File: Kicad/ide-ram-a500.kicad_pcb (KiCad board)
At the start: 2 copper layers, 82.5 x 34.9 mm, 27 parts, among them J1 power, J2 LED, J3 LED2, J4 INT2OVR, J5 INT2, J6 JTAG, J7 IDE, U1 68000D socket, U2 XC95144XL-TQ100, U3 SPX3819M5-L-3-3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

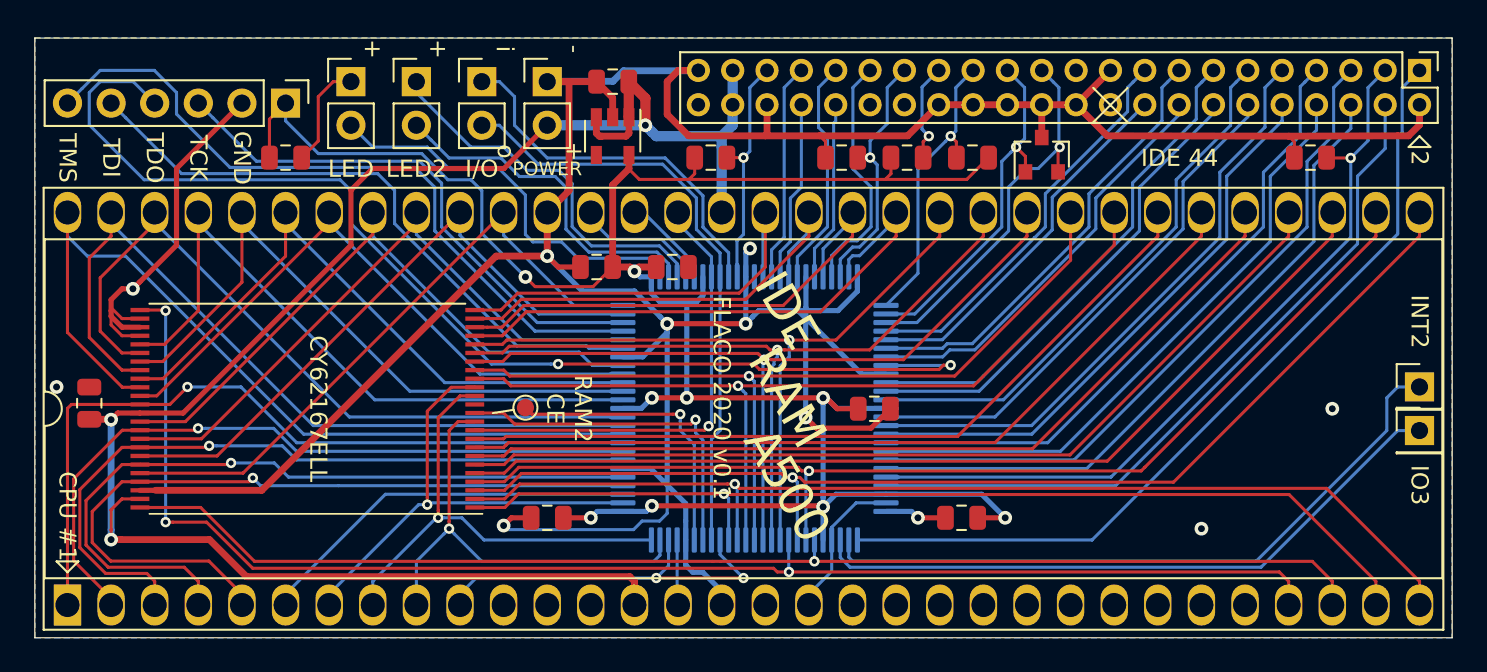
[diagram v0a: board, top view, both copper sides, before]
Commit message: Updated CPLD code with new autoconfig, new ranger-maprom, rewritten IDE ; new MapROM software ; 0.2 hardware
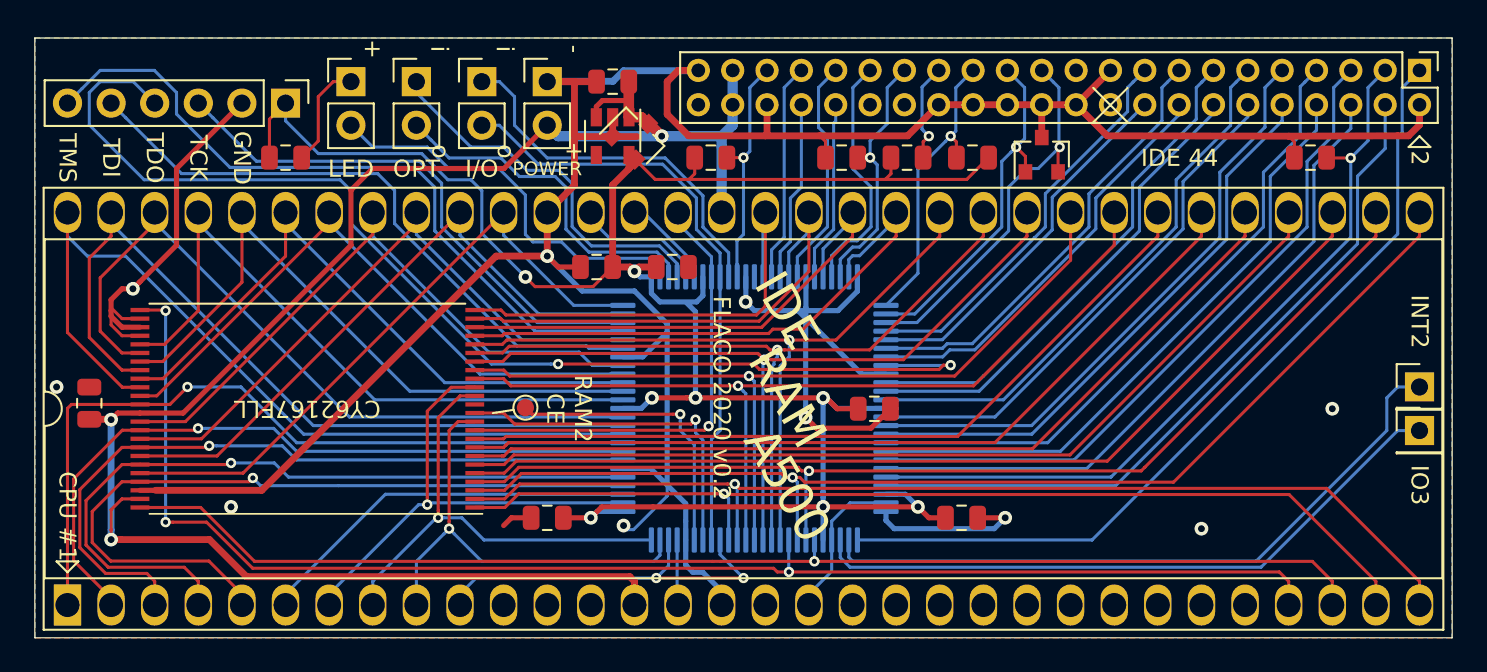
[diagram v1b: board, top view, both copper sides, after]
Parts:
- added U13: XC6206PxxxMR, Package_TO_SOT_SMD:SOT-23, F.Cu at (139.2, 81.3)
- turned C1 to 0 degrees
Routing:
- net GND: track 229.0 -> 222.5 mm, vias 11 -> 10
- net /A20: track 24.9 -> 26.5 mm
- net /A19: track 27.1 -> 28.4 mm
- net +3V3: track 130.9 -> 130.8 mm, vias 9 -> 8
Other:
- board text added: "FLACO 2020 v0.2"
- board text added: "OPT"
- board text removed: "FLACO 2020 v0.1"
- board text removed: "LED2"
